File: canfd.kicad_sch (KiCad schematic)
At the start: 5 parts, among them U7 MCP251863, X1 CSX-750P

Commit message: コンデンサを追加
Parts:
- renumbered C40 to C43, C41 to C47, R52 to R33, U7 to U6
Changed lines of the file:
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@@
   (symbol (lib_id "Device:C") (at 162.56 99.06 0) (unit 1)
     (in_bom yes) (on_board yes) (dnp no)
-    (property "Reference" "C41" (at 165.481 97.8916 0)
+    (property "Reference" "C47" (at 165.481 97.8916 0)
       (effects (font (size 1.27 1.27)) (justify left))
     )
@@
       (project "mainboard2"
         (path "/106e5476-7cb9-4c2e-b827-12558fe0d8df/33fff099-ce3b-49fb-b4f9-810325d1423e"
-          (reference "C41") (unit 1)
+          (reference "C47") (unit 1)
         )
       )
@@
   (symbol (lib_id "CAN:MCP251863") (at 120.65 101.6 0) (unit 1)
     (in_bom yes) (on_board yes) (dnp no) (fields_autoplaced)
-    (property "Reference" "U7" (at 120.65 77.47 0)
+    (property "Reference" "U6" (at 120.65 77.47 0)
       (effects (font (size 1.27 1.27)))
     )
@@
       (project "mainboard2"
         (path "/106e5476-7cb9-4c2e-b827-12558fe0d8df/33fff099-ce3b-49fb-b4f9-810325d1423e"
-          (reference "U7") (unit 1)
+          (reference "U6") (unit 1)
         )
       )
@@
   (symbol (lib_id "Device:R") (at 179.07 78.74 270) (unit 1)
     (in_bom yes) (on_board yes) (dnp no) (fields_autoplaced)
-    (property "Reference" "R52" (at 179.07 72.39 90)
+    (property "Reference" "R33" (at 179.07 72.39 90)
       (effects (font (size 1.27 1.27)))
     )
@@
       (project "mainboard2"
         (path "/106e5476-7cb9-4c2e-b827-12558fe0d8df/33fff099-ce3b-49fb-b4f9-810325d1423e"
-          (reference "R52") (unit 1)
+          (reference "R33") (unit 1)
         )
       )
@@
   (symbol (lib_id "Device:C") (at 102.87 121.92 0) (unit 1)
     (in_bom yes) (on_board yes) (dnp no) (fields_autoplaced)
-    (property "Reference" "C40" (at 106.68 120.65 0)
+    (property "Reference" "C43" (at 106.68 120.65 0)
       (effects (font (size 1.27 1.27)) (justify left))
     )
@@
       (project "mainboard2"
         (path "/106e5476-7cb9-4c2e-b827-12558fe0d8df/33fff099-ce3b-49fb-b4f9-810325d1423e"
-          (reference "C40") (unit 1)
-        )
-      )
+          (reference "C43") (unit 1)
+        )
+      )

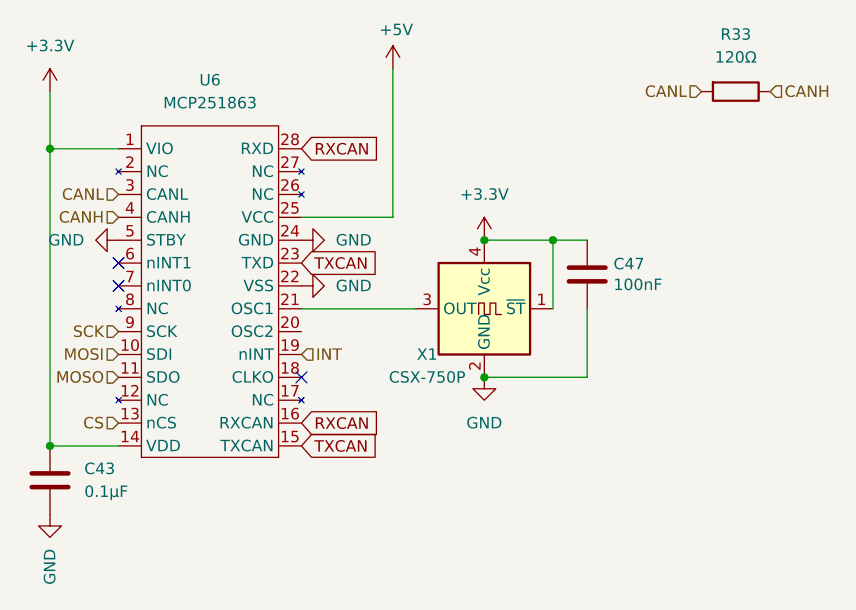
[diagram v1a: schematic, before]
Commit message: 電流センサー変更
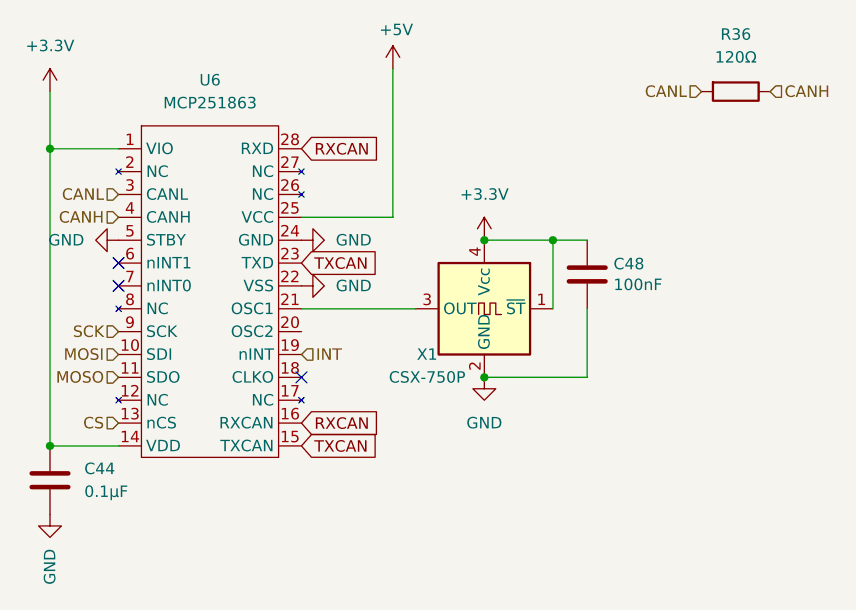
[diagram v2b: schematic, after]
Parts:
- renumbered C43 to C44, C47 to C48, R33 to R36
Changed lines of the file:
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@@
   (symbol (lib_id "power:GND") (at 130.81 95.25 90) (unit 1)
     (in_bom yes) (on_board yes) (dnp no) (fields_autoplaced)
-    (property "Reference" "#PWR0119" (at 137.16 95.25 0)
+    (property "Reference" "#PWR0122" (at 137.16 95.25 0)
       (effects (font (size 1.27 1.27)) hide)
     )
@@
       (project "mainboard2"
         (path "/106e5476-7cb9-4c2e-b827-12558fe0d8df/33fff099-ce3b-49fb-b4f9-810325d1423e"
-          (reference "#PWR0119") (unit 1)
+          (reference "#PWR0122") (unit 1)
         )
       )
@@
   (symbol (lib_id "power:+3.3V") (at 151.13 95.25 0) (unit 1)
     (in_bom yes) (on_board yes) (dnp no) (fields_autoplaced)
-    (property "Reference" "#PWR0122" (at 151.13 99.06 0)
+    (property "Reference" "#PWR0125" (at 151.13 99.06 0)
       (effects (font (size 1.27 1.27)) hide)
     )
@@
       (project "mainboard2"
         (path "/106e5476-7cb9-4c2e-b827-12558fe0d8df/33fff099-ce3b-49fb-b4f9-810325d1423e"
-          (reference "#PWR0122") (unit 1)
+          (reference "#PWR0125") (unit 1)
         )
       )
@@
   (symbol (lib_id "Device:C") (at 162.56 99.06 0) (unit 1)
     (in_bom yes) (on_board yes) (dnp no)
-    (property "Reference" "C47" (at 165.481 97.8916 0)
+    (property "Reference" "C48" (at 165.481 97.8916 0)
       (effects (font (size 1.27 1.27)) (justify left))
     )
@@
       (project "mainboard2"
         (path "/106e5476-7cb9-4c2e-b827-12558fe0d8df/33fff099-ce3b-49fb-b4f9-810325d1423e"
-          (reference "C47") (unit 1)
+          (reference "C48") (unit 1)
         )
       )
@@
   (symbol (lib_id "power:GND") (at 130.81 100.33 90) (unit 1)
     (in_bom yes) (on_board yes) (dnp no)
-    (property "Reference" "#PWR0120" (at 137.16 100.33 0)
+    (property "Reference" "#PWR0123" (at 137.16 100.33 0)
       (effects (font (size 1.27 1.27)) hide)
     )
@@
       (project "mainboard2"
         (path "/106e5476-7cb9-4c2e-b827-12558fe0d8df/33fff099-ce3b-49fb-b4f9-810325d1423e"
-          (reference "#PWR0120") (unit 1)
+          (reference "#PWR0123") (unit 1)
         )
       )
@@
   (symbol (lib_id "power:+5V") (at 140.97 76.2 0) (unit 1)
     (in_bom yes) (on_board yes) (dnp no)
-    (property "Reference" "#PWR0121" (at 140.97 80.01 0)
+    (property "Reference" "#PWR0124" (at 140.97 80.01 0)
       (effects (font (size 1.27 1.27)) hide)
     )
@@
       (project "mainboard2"
         (path "/106e5476-7cb9-4c2e-b827-12558fe0d8df/33fff099-ce3b-49fb-b4f9-810325d1423e"
-          (reference "#PWR0121") (unit 1)
+          (reference "#PWR0124") (unit 1)
         )
       )
@@
   (symbol (lib_id "Device:R") (at 179.07 78.74 270) (unit 1)
     (in_bom yes) (on_board yes) (dnp no) (fields_autoplaced)
-    (property "Reference" "R33" (at 179.07 72.39 90)
+    (property "Reference" "R36" (at 179.07 72.39 90)
       (effects (font (size 1.27 1.27)))
     )
@@
       (project "mainboard2"
         (path "/106e5476-7cb9-4c2e-b827-12558fe0d8df/33fff099-ce3b-49fb-b4f9-810325d1423e"
-          (reference "R33") (unit 1)
+          (reference "R36") (unit 1)
         )
       )
@@
   (symbol (lib_id "power:+3.3V") (at 102.87 78.74 0) (unit 1)
     (in_bom yes) (on_board yes) (dnp no) (fields_autoplaced)
-    (property "Reference" "#PWR0116" (at 102.87 82.55 0)
+    (property "Reference" "#PWR0119" (at 102.87 82.55 0)
       (effects (font (size 1.27 1.27)) hide)
     )
@@
       (project "mainboard2"
         (path "/106e5476-7cb9-4c2e-b827-12558fe0d8df/33fff099-ce3b-49fb-b4f9-810325d1423e"
-          (reference "#PWR0116") (unit 1)
+          (reference "#PWR0119") (unit 1)
         )
       )
@@
   (symbol (lib_id "power:GND") (at 110.49 95.25 270) (unit 1)
     (in_bom yes) (on_board yes) (dnp no) (fields_autoplaced)
-    (property "Reference" "#PWR0118" (at 104.14 95.25 0)
+    (property "Reference" "#PWR0121" (at 104.14 95.25 0)
       (effects (font (size 1.27 1.27)) hide)
     )
@@
       (project "mainboard2"
         (path "/106e5476-7cb9-4c2e-b827-12558fe0d8df/33fff099-ce3b-49fb-b4f9-810325d1423e"
-          (reference "#PWR0118") (unit 1)
+          (reference "#PWR0121") (unit 1)
         )
       )
@@
   (symbol (lib_id "power:GND") (at 102.87 125.73 0) (unit 1)
     (in_bom yes) (on_board yes) (dnp no)
-    (property "Reference" "#PWR0117" (at 102.87 132.08 0)
+    (property "Reference" "#PWR0120" (at 102.87 132.08 0)
       (effects (font (size 1.27 1.27)) hide)
     )
@@
       (project "mainboard2"
         (path "/106e5476-7cb9-4c2e-b827-12558fe0d8df/33fff099-ce3b-49fb-b4f9-810325d1423e"
-          (reference "#PWR0117") (unit 1)
+          (reference "#PWR0120") (unit 1)
         )
       )
@@
   (symbol (lib_id "Device:C") (at 102.87 121.92 0) (unit 1)
     (in_bom yes) (on_board yes) (dnp no) (fields_autoplaced)
-    (property "Reference" "C43" (at 106.68 120.65 0)
+    (property "Reference" "C44" (at 106.68 120.65 0)
       (effects (font (size 1.27 1.27)) (justify left))
     )
@@
       (project "mainboard2"
         (path "/106e5476-7cb9-4c2e-b827-12558fe0d8df/33fff099-ce3b-49fb-b4f9-810325d1423e"
-          (reference "C43") (unit 1)
+          (reference "C44") (unit 1)
         )
       )
@@
   (symbol (lib_id "power:GND") (at 151.13 110.49 0) (unit 1)
     (in_bom yes) (on_board yes) (dnp no) (fields_autoplaced)
-    (property "Reference" "#PWR0123" (at 151.13 116.84 0)
+    (property "Reference" "#PWR0126" (at 151.13 116.84 0)
       (effects (font (size 1.27 1.27)) hide)
     )
@@
       (project "mainboard2"
         (path "/106e5476-7cb9-4c2e-b827-12558fe0d8df/33fff099-ce3b-49fb-b4f9-810325d1423e"
-          (reference "#PWR0123") (unit 1)
-        )
-      )
+          (reference "#PWR0126") (unit 1)
+        )
+      )
